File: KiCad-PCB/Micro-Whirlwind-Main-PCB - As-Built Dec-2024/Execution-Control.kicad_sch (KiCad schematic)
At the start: 15 parts, among them SW28 SW_Push_LED, SW29 SW_Push_LED, SW30 SW_Push_LED, SW31 SW_Push_LED, SW32 SW_Push_LED, SW33 SW_Push_LED, SW34 SW_Push_LED, SW35 SW_Push_LED, SW36 SW_Push_LED, SW37 SW_Push_LED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

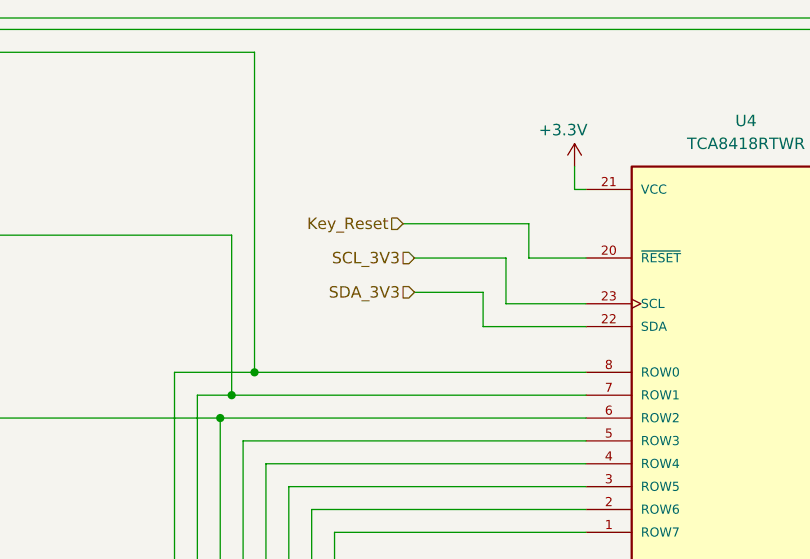
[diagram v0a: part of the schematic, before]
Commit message: I made most of the corrections to the schematic and some to the PCB. The Main PCB needs to be redone with a four-layer PCB, so I didn't re-route all the traces on the PCB The Power switch needs to be moved out of the way of the HDMI connector - that wasn't done either. See Notes/PCB-Corrections for a listing of the changes made, and the ones that are still pending   /guy
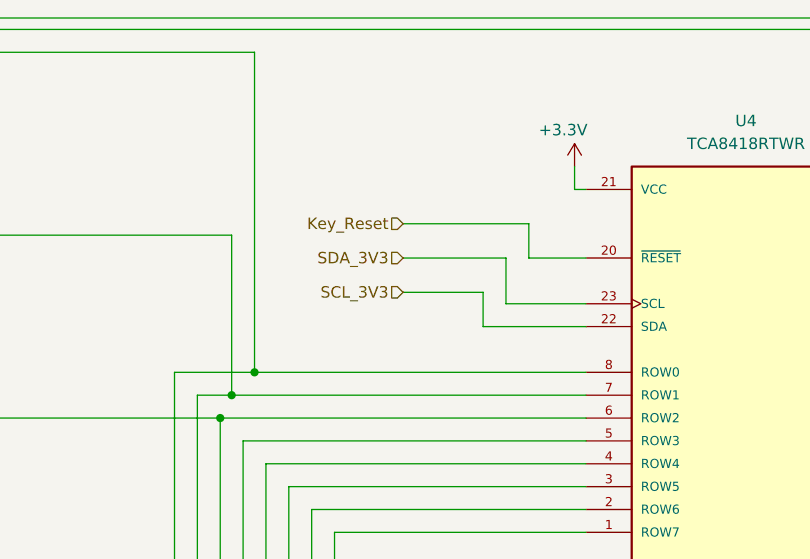
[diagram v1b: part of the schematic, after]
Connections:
- net SCL_3V3: now also U4.22 (SDA); no longer U4.23 (SCL)
- net SDA_3V3: now also U4.23 (SCL); no longer U4.22 (SDA)
